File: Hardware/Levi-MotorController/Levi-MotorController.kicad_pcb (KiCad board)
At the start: 2 copper layers, 13 parts, among them J1 RJ45, Q1 IRLB8721PBF, Q2 IRLB8721PBF, Q3 IRLB8721PBF, Q4 IRLB8721PBF

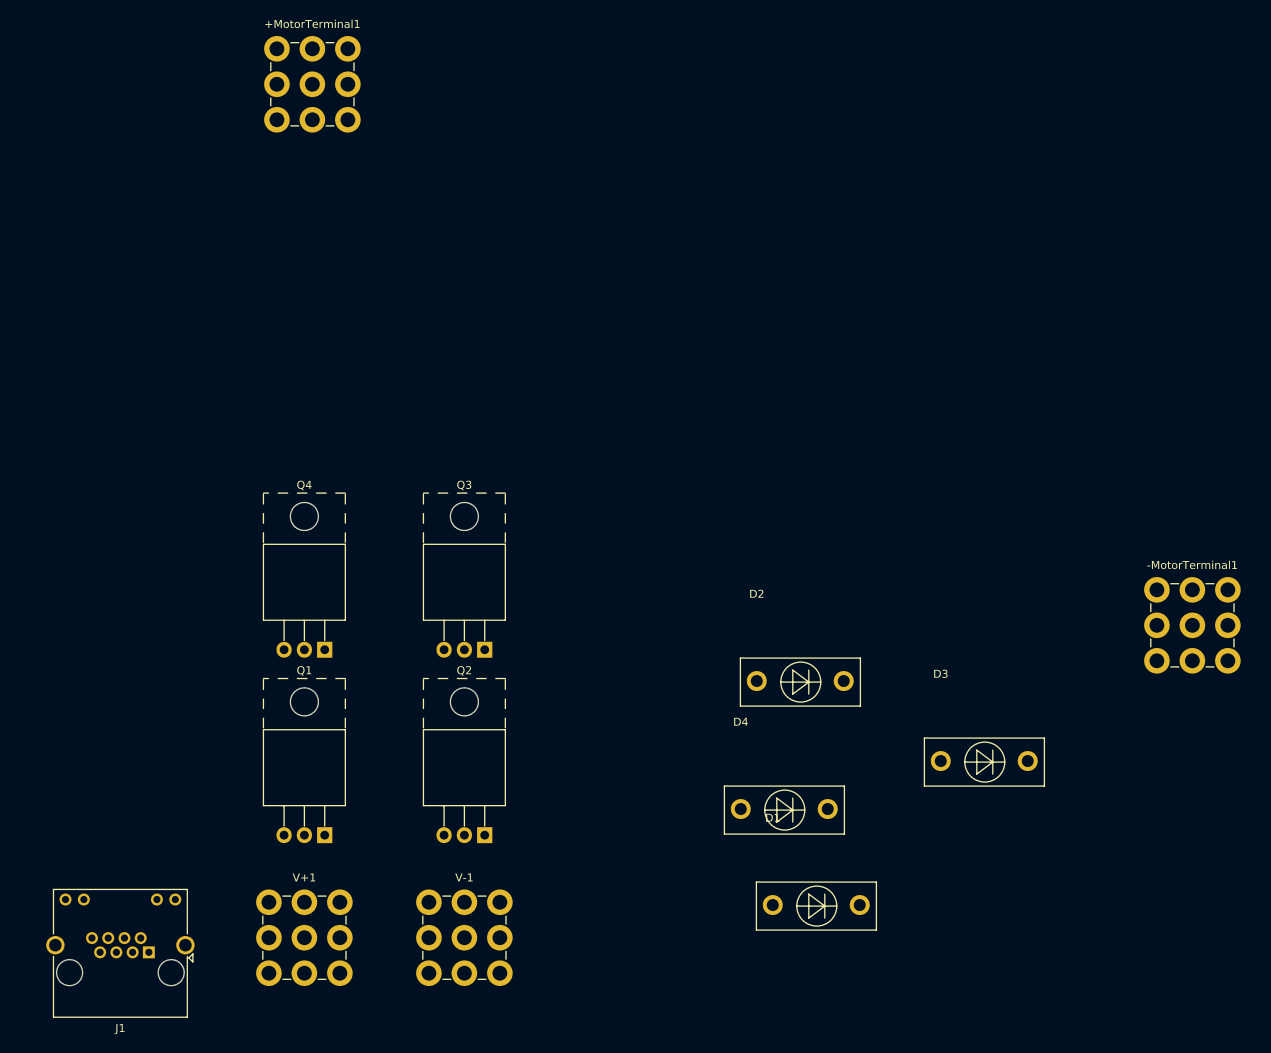
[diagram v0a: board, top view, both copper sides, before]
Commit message: Added prototype motor controller
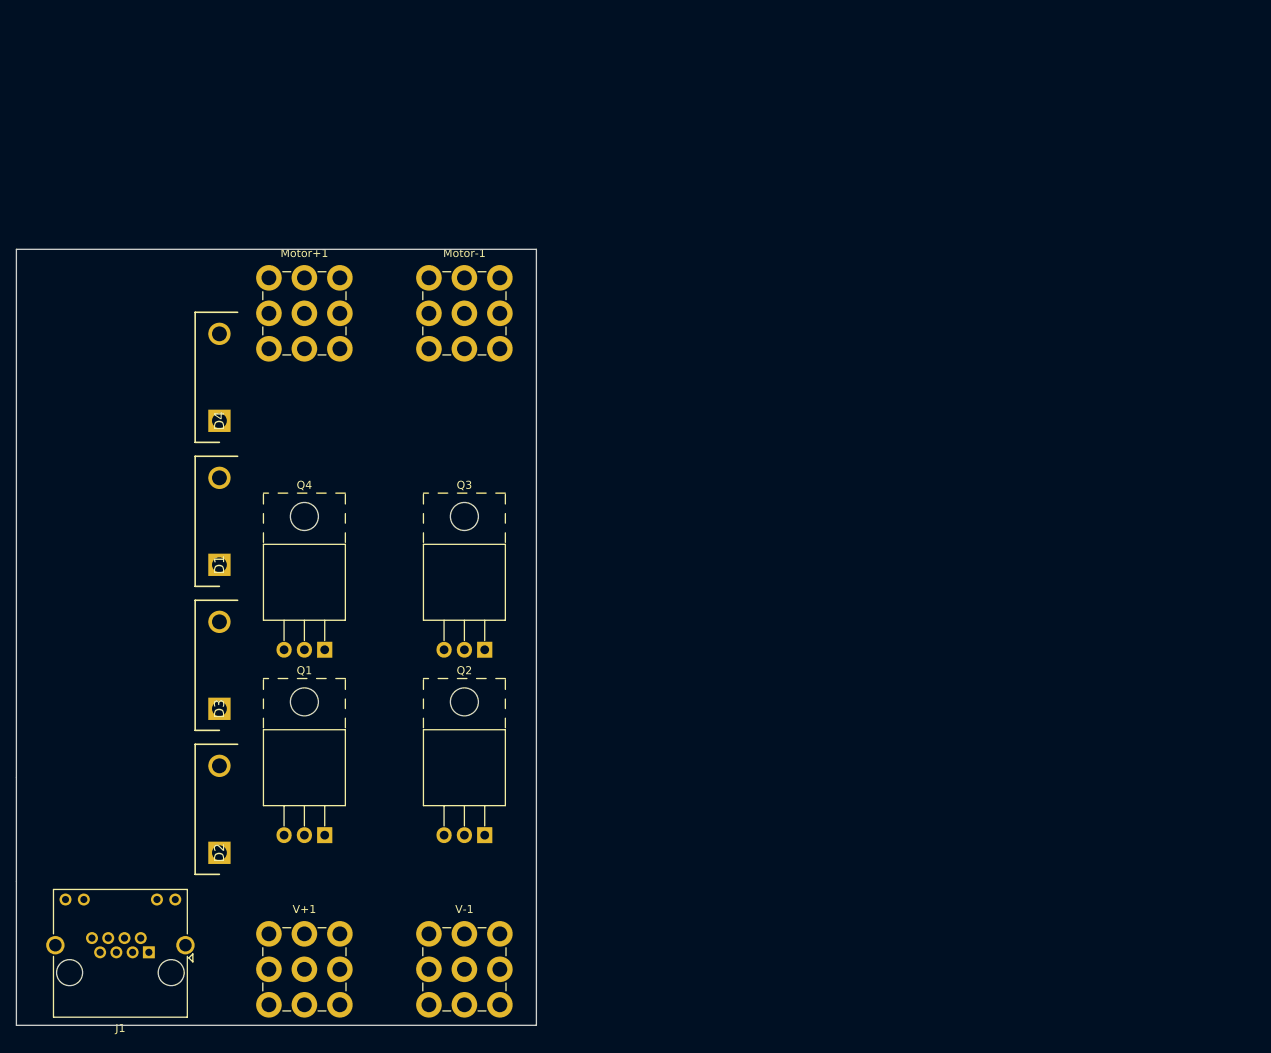
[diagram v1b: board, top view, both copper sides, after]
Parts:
- removed +MotorTerminal1, -MotorTerminal1: Screw_Terminal_01x01, TerminalBlock_Wuerth:Wuerth_REDCUBE-THR_WP-THRBU_74650195_THR
- added Motor+1: Screw_Terminal_01x01, Project_TerminalBlock_Wuerth:Wuerth_REDCUBE-THR_WP-THRSH_74651195_THR, F.Cu at (126.0, 68.0)
- added Motor-1: Screw_Terminal_01x01, Project_TerminalBlock_Wuerth:Wuerth_REDCUBE-THR_WP-THRSH_74651195_THR, F.Cu at (146.0, 68.0)
- D1, D2, D3, D4: footprint Schotty-Diode-THT:APT100S20BG -> APT100S20BG:TO1087P531X1588X2596-2P
- V+1, V-1: footprint TerminalBlock_Wuerth:Wuerth_REDCUBE-THR_WP-THRBU_74650195_THR -> Project_TerminalBlock_Wuerth:Wuerth_REDCUBE-THR_WP-THRSH_74651195_THR
- moved D3 90.3 mm to (115.4, 117.4), turned to 90 degrees
- moved D1 76.1 mm to (115.4, 99.4), turned to 90 degrees
- moved D4 75.3 mm to (115.4, 81.4), turned to 90 degrees
- moved D2 74.5 mm to (115.4, 135.4), turned to 90 degrees
- moved V+1 3.95 mm to (126.0, 150.0)
- moved V-1 3.95 mm to (146.0, 150.0)
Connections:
- D1 pad 1: Net-(V-1-Pad1) -> Net-(D1-Pad1)
- D1 pad 2: Net-(+MotorTerminal1-Pad1) -> Net-(Q1-Pad3)
- D2 pad 1: Net-(V-1-Pad1) -> Net-(D2-Pad1)
- D2 pad 2: Net-(-MotorTerminal1-Pad1) -> Net-(Q1-Pad3)
- D3 pad 1: Net-(+MotorTerminal1-Pad1) -> Net-(Q3-Pad2)
- D3 pad 2: Net-(V+1-Pad1) -> Net-(D1-Pad1)
- D4 pad 1: Net-(-MotorTerminal1-Pad1) -> Net-(Q3-Pad2)
- D4 pad 2: Net-(V+1-Pad1) -> Net-(D2-Pad1)
- Q1 pad 2: Net-(+MotorTerminal1-Pad1) -> Net-(D1-Pad1)
- Q1 pad 3: Net-(V-1-Pad1) -> Net-(Q1-Pad3)
- Q2 pad 2: Net-(-MotorTerminal1-Pad1) -> Net-(D2-Pad1)
- Q2 pad 3: Net-(V-1-Pad1) -> Net-(Q1-Pad3)
- Q3 pad 2: Net-(V+1-Pad1) -> Net-(Q3-Pad2)
- Q3 pad 3: Net-(+MotorTerminal1-Pad1) -> Net-(D1-Pad1)
- Q4 pad 2: Net-(V+1-Pad1) -> Net-(Q3-Pad2)
- Q4 pad 3: Net-(-MotorTerminal1-Pad1) -> Net-(D2-Pad1)
- V+1 pad 1: Net-(V+1-Pad1) -> Net-(Q3-Pad2)
- V-1 pad 1: Net-(V-1-Pad1) -> Net-(Q1-Pad3)
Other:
- board outline added: 65 x 97 mm
